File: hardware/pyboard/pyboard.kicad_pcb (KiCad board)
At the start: 2 copper layers, 65 parts, among them J1 Battery, J2 Arduino_Mega2560_Shield, J6 USB_B_Micro, J9 Micro_SD_SCHA5B0200, Q1 IRLML6402, Q2 IRLML6402, SW1 RST, SW2 USR, U1 STM32F405RGT6, U2 MCP1703A-3302_SOT89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

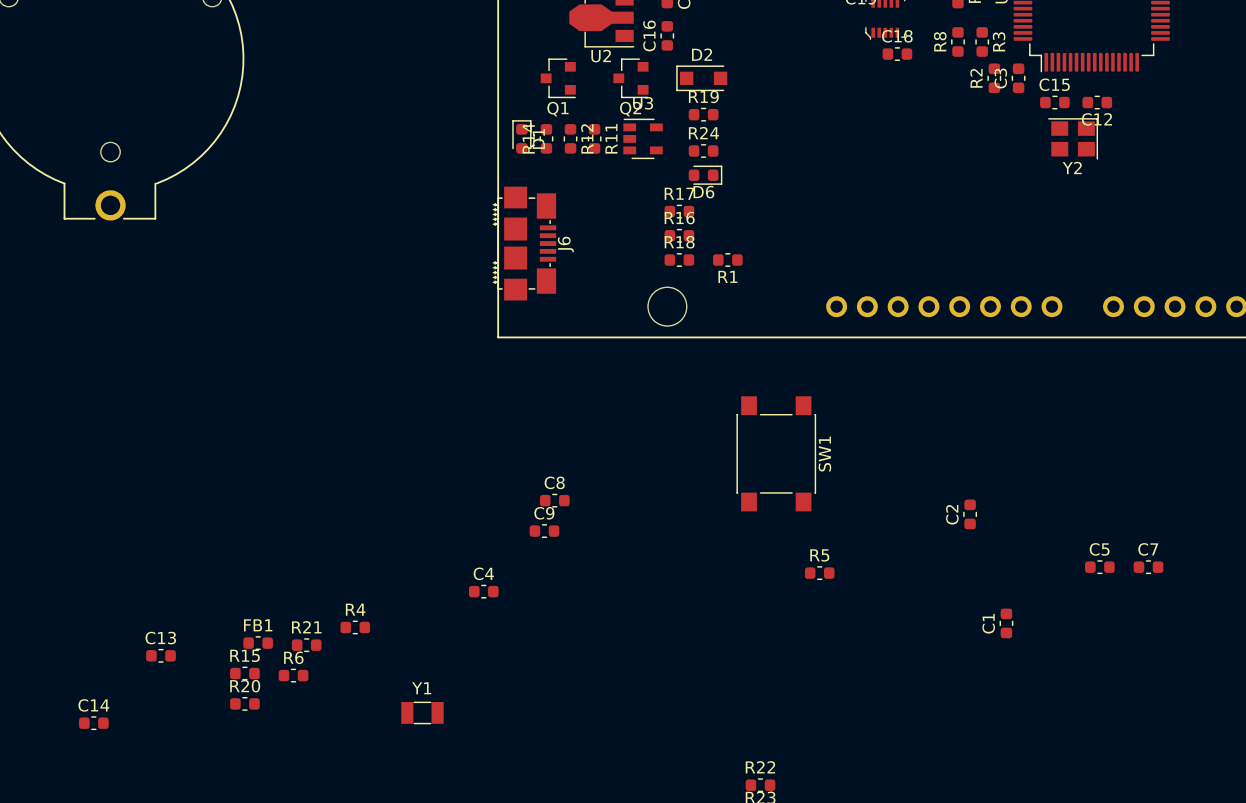
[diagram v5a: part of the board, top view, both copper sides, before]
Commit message: Place both crystal oscillators
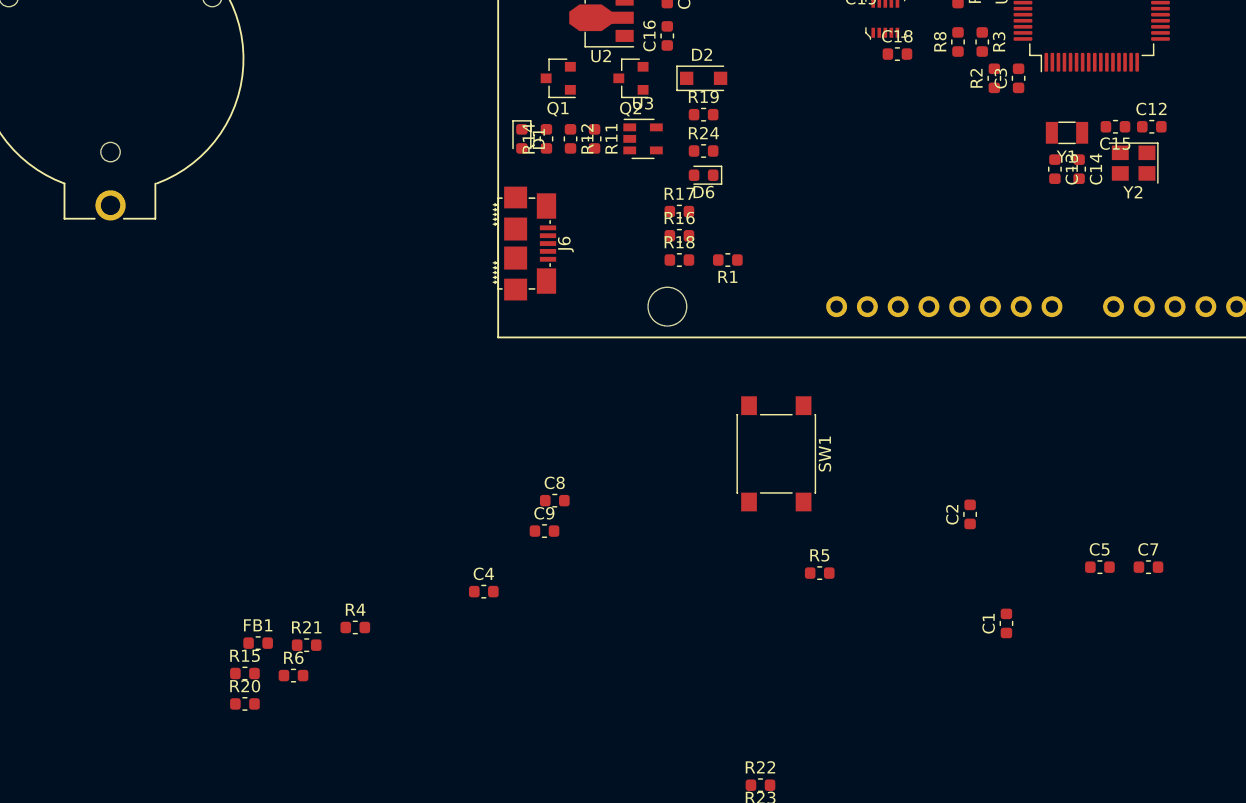
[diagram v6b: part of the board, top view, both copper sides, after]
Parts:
- moved C14 93.3 mm to (148.0, 106.1), turned to 270 degrees
- moved C13 84.0 mm to (146.0, 106.1), turned to 270 degrees
- moved Y1 71.6 mm to (147.0, 103.1), turned to 180 degrees
- moved C15 5.39 mm to (151.0, 102.6), turned to 180 degrees
- moved Y2 5.39 mm to (152.5, 105.6)
- moved C12 4.92 mm to (154.0, 102.6), turned to 0 degrees
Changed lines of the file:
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@@
     (thickness 1.6)
     (drawings 0)
-    (tracks 0)
+    (tracks 1)
     (zones 0)
     (modules 65)
@@
   )
   (module Capacitor_SMD:C_0603_1608Metric (layer F.Cu)
-    (at 149.46 100.61 180)
+    (at 153.96 102.61)
     (descr "Capacitor SMD 0603 (1608 Metric), square (rectangular) end terminal, IPC_7351 nominal, (Body size source: http://www.tortai-tech.com/upload/download/2011102023233369053.pdf), generated with kicad-footprint-generator")
     (tags capacitor)
@@
       (effects (font (size 0.4 0.4) (thickness 0.06)))
     )
-    (pad 1 smd roundrect (at -0.7875 0 180) (size 0.875 0.95) (layers F.Cu F.Paste F.Mask) (roundrect_rratio 0.25)
+    (pad 1 smd roundrect (at -0.7875 0) (size 0.875 0.95) (layers F.Cu F.Paste F.Mask) (roundrect_rratio 0.25)
       (net 1 GND))
-    (pad 2 smd roundrect (at 0.7875 0 180) (size 0.875 0.95) (layers F.Cu F.Paste F.Mask) (roundrect_rratio 0.25)
+    (pad 2 smd roundrect (at 0.7875 0) (size 0.875 0.95) (layers F.Cu F.Paste F.Mask) (roundrect_rratio 0.25)
       (net 8 "Net-(C12-Pad2)"))
     (model ${KISYS3DMOD}/Capacitor_SMD.3dshapes/C_0603_1608Metric.wrl
@@
   )
   (module Capacitor_SMD:C_0603_1608Metric (layer F.Cu)
-    (at 72.165001 146.285001)
+    (at 145.96 106.11 270)
     (descr "Capacitor SMD 0603 (1608 Metric), square (rectangular) end terminal, IPC_7351 nominal, (Body size source: http://www.tortai-tech.com/upload/download/2011102023233369053.pdf), generated with kicad-footprint-generator")
     (tags capacitor)
     (attr smd)
-    (fp_text reference C13 (at 0 -1.43) (layer F.SilkS)
+    (fp_text reference C13 (at 0 -1.43 90) (layer F.SilkS)
       (effects (font (size 1 1) (thickness 0.15)))
     )
-    (fp_text value 20pF (at 0 1.43) (layer F.Fab)
+    (fp_text value 20pF (at 0 1.43 90) (layer F.Fab)
       (effects (font (size 1 1) (thickness 0.15)))
     )
@@
     (fp_line (start 1.48 -0.73) (end 1.48 0.73) (layer F.CrtYd) (width 0.05))
     (fp_line (start 1.48 0.73) (end -1.48 0.73) (layer F.CrtYd) (width 0.05))
-    (fp_text user %R (at 0 0) (layer F.Fab)
+    (fp_text user %R (at 0 0 90) (layer F.Fab)
       (effects (font (size 0.4 0.4) (thickness 0.06)))
     )
-    (pad 1 smd roundrect (at -0.7875 0) (size 0.875 0.95) (layers F.Cu F.Paste F.Mask) (roundrect_rratio 0.25)
+    (pad 1 smd roundrect (at -0.7875 0 270) (size 0.875 0.95) (layers F.Cu F.Paste F.Mask) (roundrect_rratio 0.25)
       (net 9 /N1))
-    (pad 2 smd roundrect (at 0.7875 0) (size 0.875 0.95) (layers F.Cu F.Paste F.Mask) (roundrect_rratio 0.25)
+    (pad 2 smd roundrect (at 0.7875 0 270) (size 0.875 0.95) (layers F.Cu F.Paste F.Mask) (roundrect_rratio 0.25)
       (net 1 GND))
     (model ${KISYS3DMOD}/Capacitor_SMD.3dshapes/C_0603_1608Metric.wrl
@@
   )
   (module Capacitor_SMD:C_0603_1608Metric (layer F.Cu)
-    (at 66.625001 151.845001)
+    (at 147.96 106.11 270)
     (descr "Capacitor SMD 0603 (1608 Metric), square (rectangular) end terminal, IPC_7351 nominal, (Body size source: http://www.tortai-tech.com/upload/download/2011102023233369053.pdf), generated with kicad-footprint-generator")
     (tags capacitor)
     (attr smd)
-    (fp_text reference C14 (at 0 -1.43) (layer F.SilkS)
+    (fp_text reference C14 (at 0 -1.43 90) (layer F.SilkS)
       (effects (font (size 1 1) (thickness 0.15)))
     )
-    (fp_text value 20pF (at 0 1.43) (layer F.Fab)
+    (fp_text value 20pF (at 0 1.43 90) (layer F.Fab)
       (effects (font (size 1 1) (thickness 0.15)))
     )
@@
     (fp_line (start 1.48 -0.73) (end 1.48 0.73) (layer F.CrtYd) (width 0.05))
     (fp_line (start 1.48 0.73) (end -1.48 0.73) (layer F.CrtYd) (width 0.05))
-    (fp_text user %R (at 0 0) (layer F.Fab)
+    (fp_text user %R (at 0 0 90) (layer F.Fab)
       (effects (font (size 0.4 0.4) (thickness 0.06)))
     )
-    (pad 1 smd roundrect (at -0.7875 0) (size 0.875 0.95) (layers F.Cu F.Paste F.Mask) (roundrect_rratio 0.25)
+    (pad 1 smd roundrect (at -0.7875 0 270) (size 0.875 0.95) (layers F.Cu F.Paste F.Mask) (roundrect_rratio 0.25)
       (net 10 /N2))
-    (pad 2 smd roundrect (at 0.7875 0) (size 0.875 0.95) (layers F.Cu F.Paste F.Mask) (roundrect_rratio 0.25)
+    (pad 2 smd roundrect (at 0.7875 0 270) (size 0.875 0.95) (layers F.Cu F.Paste F.Mask) (roundrect_rratio 0.25)
       (net 1 GND))
     (model ${KISYS3DMOD}/Capacitor_SMD.3dshapes/C_0603_1608Metric.wrl
@@
   )
   (module Capacitor_SMD:C_0603_1608Metric (layer F.Cu)
-    (at 145.96 100.61)
+    (at 150.96 102.61 180)
     (descr "Capacitor SMD 0603 (1608 Metric), square (rectangular) end terminal, IPC_7351 nominal, (Body size source: http://www.tortai-tech.com/upload/download/2011102023233369053.pdf), generated with kicad-footprint-generator")
     (tags capacitor)
@@
     (fp_line (start -0.8 -0.4) (end 0.8 -0.4) (layer F.Fab) (width 0.1))
     (fp_line (start -0.8 0.4) (end -0.8 -0.4) (layer F.Fab) (width 0.1))
-    (pad 2 smd roundrect (at 0.7875 0) (size 0.875 0.95) (layers F.Cu F.Paste F.Mask) (roundrect_rratio 0.25)
+    (pad 2 smd roundrect (at 0.7875 0 180) (size 0.875 0.95) (layers F.Cu F.Paste F.Mask) (roundrect_rratio 0.25)
       (net 11 "Net-(C15-Pad2)"))
-    (pad 1 smd roundrect (at -0.7875 0) (size 0.875 0.95) (layers F.Cu F.Paste F.Mask) (roundrect_rratio 0.25)
+    (pad 1 smd roundrect (at -0.7875 0 180) (size 0.875 0.95) (layers F.Cu F.Paste F.Mask) (roundrect_rratio 0.25)
       (net 1 GND))
     (model ${KISYS3DMOD}/Capacitor_SMD.3dshapes/C_0603_1608Metric.wrl
@@
   )
   (module Crystal:Crystal_SMD_3215-2Pin_3.2x1.5mm (layer F.Cu)
-    (at 93.75 151)
+    (at 146.96 103.11 180)
     (descr "SMD Crystal FC-135 https://support.epson.biz/td/api/doc_check.php?dl=brief_FC-135R_en.pdf")
     (tags "SMD SMT Crystal")
@@
     (fp_line (start -2 -1.15) (end -2 1.15) (layer F.CrtYd) (width 0.05))
     (fp_line (start 2 -1.15) (end 2 1.15) (layer F.CrtYd) (width 0.05))
-    (pad 1 smd rect (at 1.25 0) (size 1 1.8) (layers F.Cu F.Paste F.Mask)
+    (pad 1 smd rect (at 1.25 0 180) (size 1 1.8) (layers F.Cu F.Paste F.Mask)
       (net 9 /N1))
-    (pad 2 smd rect (at -1.25 0) (size 1 1.8) (layers F.Cu F.Paste F.Mask)
+    (pad 2 smd rect (at -1.25 0 180) (size 1 1.8) (layers F.Cu F.Paste F.Mask)
       (net 10 /N2))
     (model ${KISYS3DMOD}/Crystal.3dshapes/Crystal_SMD_3215-2Pin_3.2x1.5mm.wrl
@@
   )
   (module Crystal:Crystal_SMD_3225-4Pin_3.2x2.5mm (layer F.Cu)
-    (at 147.46 103.61 180)
+    (at 152.46 105.61 180)
     (descr "SMD Crystal SERIES SMD3225/4 http://www.txccrystal.com/images/pdf/7m-accuracy.pdf, 3.2x2.5mm^2 package")
     (tags "SMD SMT crystal")
@@
     )
   )
+  (segment (start 153.66 104.76) (end 153.56 104.76) (width 0.25) (layer F.Cu) (net 8))
 )

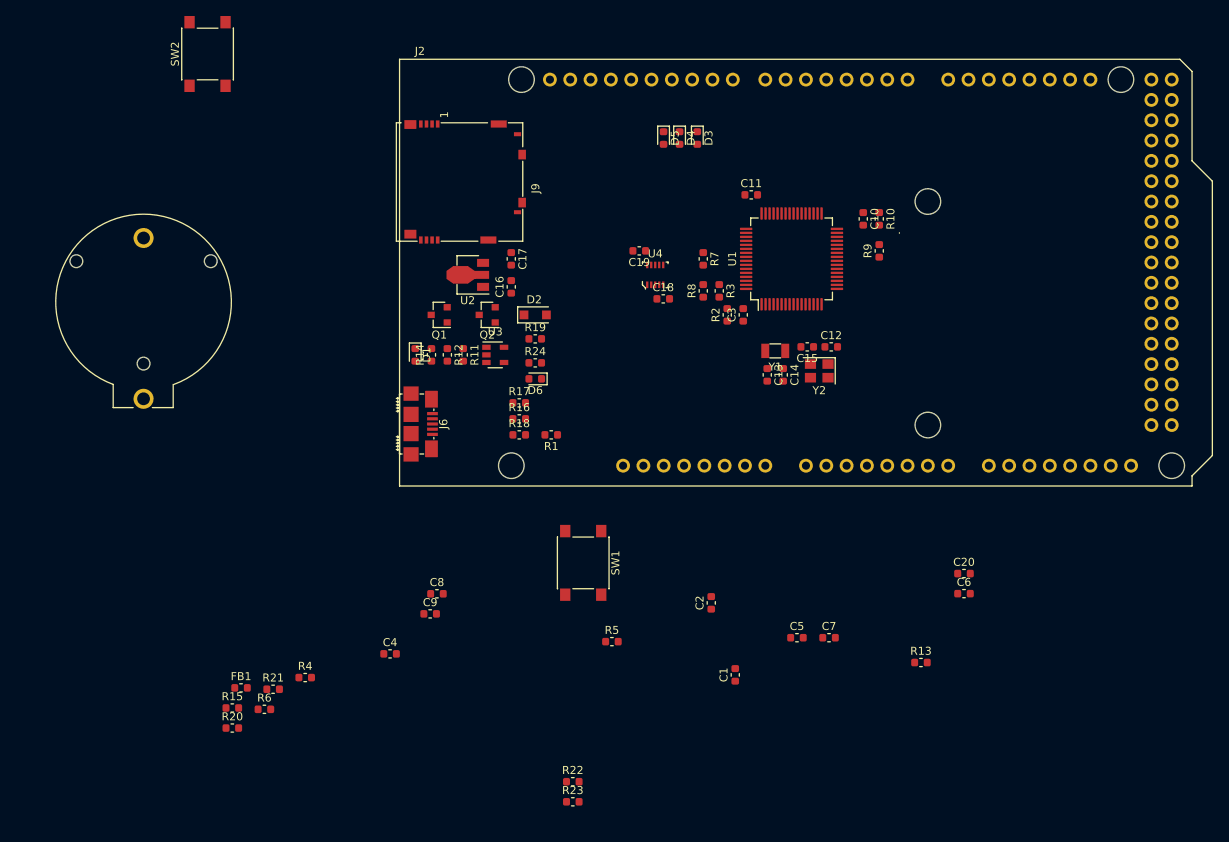
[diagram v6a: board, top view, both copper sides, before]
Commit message: Change X18 pin binding
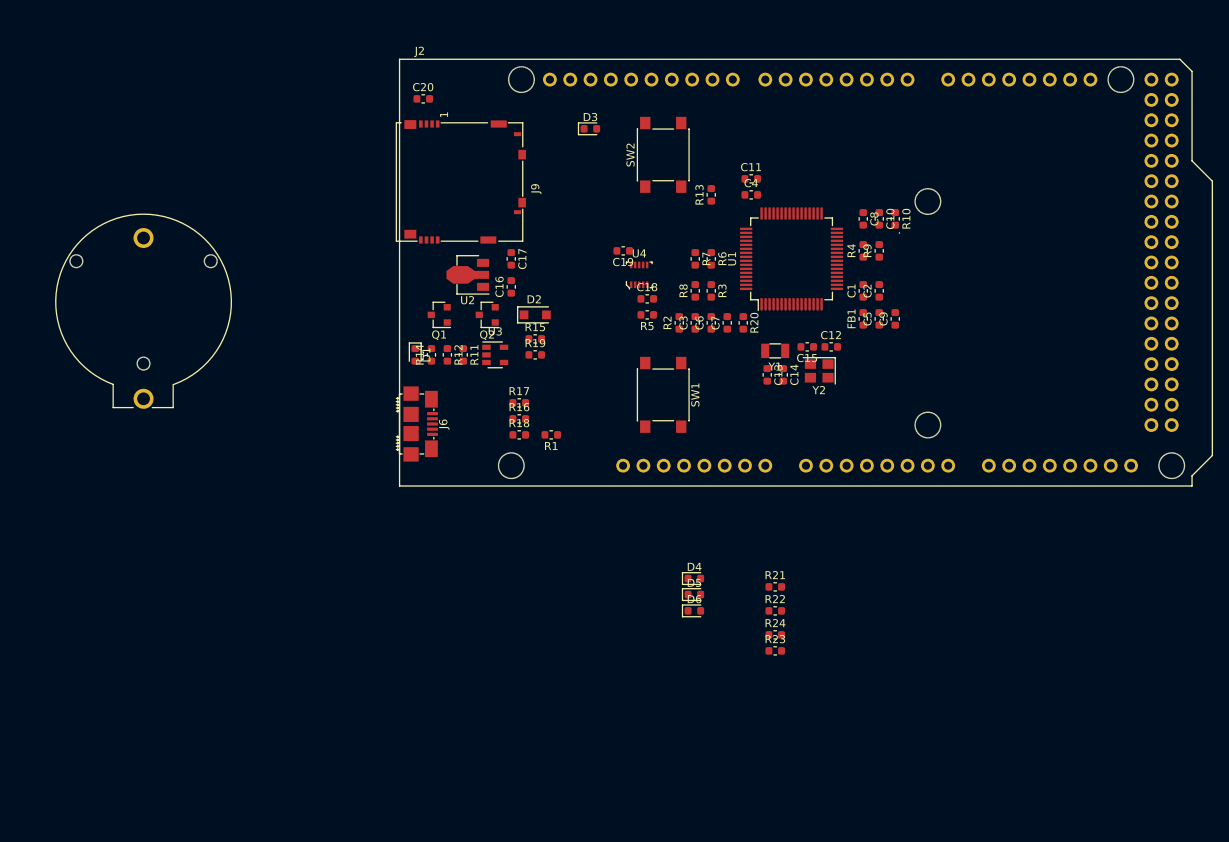
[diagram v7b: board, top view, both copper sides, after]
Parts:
- moved FB1 90.4 mm to (158.0, 99.1), turned to 90 degrees
- moved C20 89.9 mm to (103.0, 71.6)
- moved R4 87.8 mm to (158.0, 90.6), turned to 90 degrees
- moved R20 81.5 mm to (143.0, 99.6), turned to 270 degrees
- moved R6 79.3 mm to (139.0, 91.6), turned to 270 degrees
- moved C4 73.0 mm to (144.0, 83.6)
- moved C8 71.0 mm to (158.0, 86.6), turned to 270 degrees
- moved C9 68.8 mm to (162.0, 99.1), turned to 90 degrees
- moved R13 64.1 mm to (139.0, 83.6), turned to 90 degrees
- moved R21 64.1 mm to (147.0, 132.6)
- moved R15 59.7 mm to (117.0, 101.6)
- moved SW2 58.3 mm to (133.0, 78.6)
- moved D5 57.2 mm to (136.9, 133.6), turned to 0 degrees
- moved D4 55.1 mm to (136.9, 131.6), turned to 0 degrees
- moved C1 50.6 mm to (158.0, 95.6)
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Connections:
- J2 pad A14: Net-(J2-PadA14) -> (no net)
- J2 pad A15: Net-(J2-PadA15) -> (no net)
- J2 pad AREF: Net-(J2-PadAREF) -> (no net)
- J2 pad D10: /GRN -> /BLU
- J2 pad D11: /BLU -> /YEL
- J2 pad D12: /YEL -> /SW
- J2 pad D13: /SW -> /BOOT0
- J2 pad D16: Net-(J2-PadD16) -> (no net)
- J2 pad D17: Net-(J2-PadD17) -> (no net)
- J2 pad D18: Net-(J2-PadD18) -> (no net)
- J2 pad D19: Net-(J2-PadD19) -> (no net)
- J2 pad D22: /BOOT0 -> (no net)
- J2 pad D23: Net-(J2-PadD23) -> (no net)
- J2 pad D24: Net-(J2-PadD24) -> (no net)
- J2 pad D25: Net-(J2-PadD25) -> (no net)
- J2 pad D26: Net-(J2-PadD26) -> (no net)
- J2 pad D27: Net-(J2-PadD27) -> (no net)
- J2 pad D28: Net-(J2-PadD28) -> (no net)
- J2 pad D29: Net-(J2-PadD29) -> (no net)
- J2 pad D30: Net-(J2-PadD30) -> (no net)
- J2 pad D31: Net-(J2-PadD31) -> (no net)
- J2 pad D32: Net-(J2-PadD32) -> (no net)
- J2 pad D33: Net-(J2-PadD33) -> (no net)
- J2 pad D34: Net-(J2-PadD34) -> (no net)
- J2 pad D35: Net-(J2-PadD35) -> (no net)
- J2 pad D36: Net-(J2-PadD36) -> (no net)
- J2 pad D37: Net-(J2-PadD37) -> (no net)
- J2 pad D38: Net-(J2-PadD38) -> (no net)
- J2 pad D39: Net-(J2-PadD39) -> (no net)
- J2 pad D40: Net-(J2-PadD40) -> (no net)
- J2 pad D41: Net-(J2-PadD41) -> (no net)
- J2 pad D42: Net-(J2-PadD42) -> (no net)
- J2 pad D43: Net-(J2-PadD43) -> (no net)
- J2 pad D44: Net-(J2-PadD44) -> (no net)
- J2 pad D45: Net-(J2-PadD45) -> (no net)
- J2 pad D46: Net-(J2-PadD46) -> (no net)
- J2 pad D47: Net-(J2-PadD47) -> (no net)
- J2 pad D48: Net-(J2-PadD48) -> (no net)
- J2 pad D49: Net-(J2-PadD49) -> (no net)
- J2 pad D50: Net-(J2-PadD50) -> (no net)
- J2 pad D51: Net-(J2-PadD51) -> (no net)
- J2 pad D52: Net-(J2-PadD52) -> (no net)
- J2 pad D53: Net-(J2-PadD53) -> (no net)
- J2 pad D8: /X18 -> /RED
- J2 pad D9: /RED -> /GRN
- J2 pad IORF: Net-(J2-PadIORF) -> (no net)
- J6 pad CGND: GND -> (no net)
- J6 pad D+: /DP_USB -> (no net)
- J6 pad D-: /DM_USB -> (no net)
- J6 pad GND: GND -> (no net)
- J6 pad ID: /ID_USB -> (no net)
- J6 pad VBUS: /VBUS_USB -> (no net)
- R16 pad 1: /DP_USB -> (no net)
- R17 pad 1: /DM_USB -> (no net)
- R18 pad 1: /ID_USB -> (no net)
